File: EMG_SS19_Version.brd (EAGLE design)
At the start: 160 x 100 mm, 219 parts, among them SW1 B3S-1000, SW2 B3S-1000, SW3 B3S-1000, SW4 B3S-1000, SW5 B3S-1000, T11 OPA388, T12 OPA388, T21 OPA388, T22 OPA388

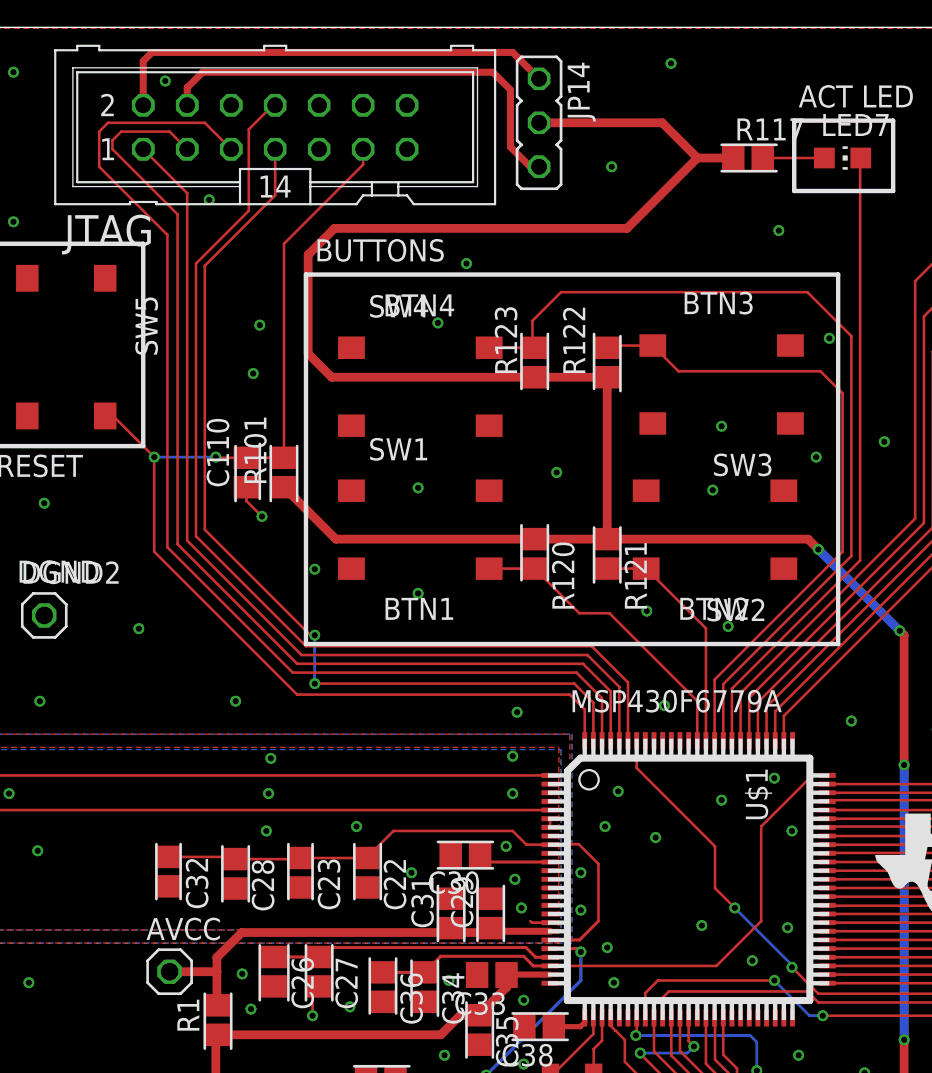
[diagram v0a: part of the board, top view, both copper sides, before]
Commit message: Fixed 3 buttons Added UART as back-channel to JTAG header acc. http://www.ti.com/lit/ug/slau647m/slau647m.pdf p.19
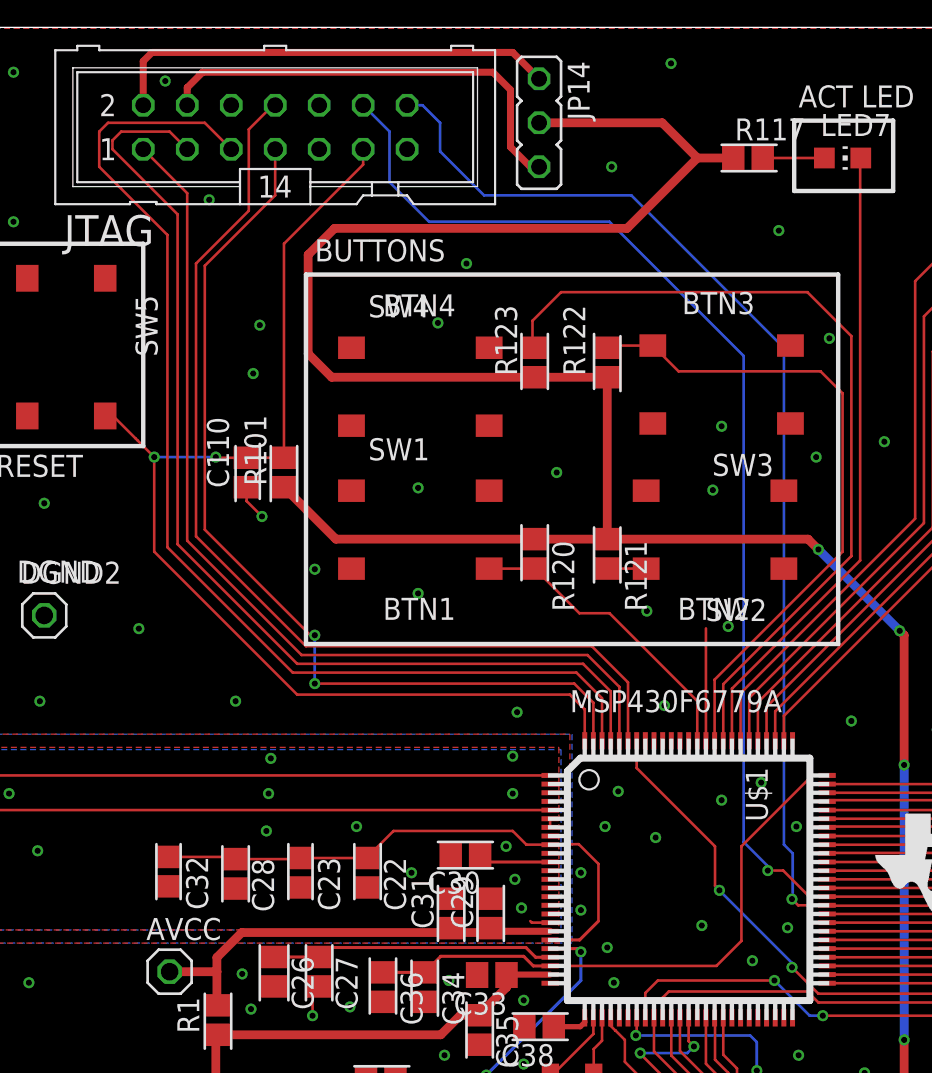
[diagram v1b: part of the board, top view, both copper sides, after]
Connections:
- removed net N$56: SW2.1
- removed net P4.1: P4.2, U$1.60
- removed net P4.2: P4.3, U$1.61
- new net UART_CTS: JTAG.10
- new net UART_RTS: JTAG.13
- new net UART_RX: JTAG.14, P4.2, U$1.60
- new net UART_TX: JTAG.12, P4.3, U$1.61
- net BTN2: now also SW2.1; no longer SW2.3
- net BTN4: now also SW4.1; no longer SW4.3
- net RESET: now also SW5.1; no longer SW5.3
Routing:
- net UART_TX: track 0.00 -> 82.7 mm, vias 0 -> 1
- net UART_RX: track 0.00 -> 82.3 mm, vias 0 -> 1
- net P4.1: track 19.5 -> 0.00 mm
- net P4.2: track 18.6 -> 0.00 mm
- net BTN2: track 13.6 -> 8.74 mm
- net BTN4: track 50.9 -> 48.6 mm
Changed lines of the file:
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@@
 <?xml version="1.0" encoding="utf-8"?>
 <!DOCTYPE eagle SYSTEM "eagle.dtd">
-<eagle version="9.4.2">
+<eagle version="9.4.1">
 <drawing>
 <settings>
@@
 <via x="117.729" y="44.958" extent="1-16" drill="0.35"/>
 <via x="132.334" y="48.133" extent="1-16" drill="0.35"/>
-<via x="137.541" y="53.594" extent="1-16" drill="0.35"/>
+<via x="137.795" y="53.848" extent="1-16" drill="0.35"/>
 <via x="133.477" y="55.372" extent="1-16" drill="0.35"/>
 <via x="145.415" y="33.782" extent="1-16" drill="0.35"/>
@@
 <via x="135.255" y="46.101" extent="1-16" drill="0.35"/>
 <via x="137.287" y="48.006" extent="1-16" drill="0.35"/>
-<via x="136.525" y="56.642" extent="1-16" drill="0.35"/>
+<via x="135.763" y="56.388" extent="1-16" drill="0.35"/>
 <via x="126.873" y="46.863" extent="1-16" drill="0.35"/>
 <via x="125.349" y="49.022" extent="1-16" drill="0.35"/>
@@
 <wire x1="124.714" y1="61.468" x2="108.966" y2="61.468" width="0.1524" layer="1"/>
 <wire x1="108.966" y1="61.468" x2="100.711" y2="69.723" width="0.1524" layer="1"/>
-<contactref element="SW5" pad="3"/>
-<wire x1="97.881" y1="77.559" x2="98.336" y2="77.559" width="0.1524" layer="1"/>
 <wire x1="98.336" y1="77.559" x2="99.649" y2="76.246" width="0.1524" layer="1"/>
+<contactref element="SW5" pad="1"/>
+<wire x1="93.381" y1="77.559" x2="98.336" y2="77.559" width="0" layer="19" extent="1-1"/>
 </signal>
 <signal name="TEST/SBWTCK">
@@
 <contactref element="R121" pad="2"/>
 <contactref element="U$1" pad="86"/>
-<contactref element="SW2" pad="3"/>
 <wire x1="126.873" y1="68.746" x2="129.118" y2="68.746" width="0.1524" layer="1"/>
-<wire x1="129.118" y1="68.746" x2="129.121" y2="68.743" width="0.1524" layer="1"/>
-<wire x1="132.572" y1="65.292" x2="129.121" y2="68.743" width="0.1524" layer="1"/>
 <wire x1="132.572" y1="58.8" x2="132.572" y2="65.292" width="0.1524" layer="1"/>
+<contactref element="SW2" pad="1"/>
+<wire x1="129.118" y1="68.746" x2="129.121" y2="73.243" width="0" layer="19" extent="1-1"/>
+<wire x1="132.572" y1="65.292" x2="129.118" y2="68.746" width="0" layer="19" extent="1-1"/>
 </signal>
 <signal name="BTN4">
@@
 <wire x1="133.572" y1="62.071" x2="140.97" y2="69.469" width="0.1524" layer="1"/>
 <wire x1="140.97" y1="69.469" x2="140.97" y2="82.169" width="0.1524" layer="1"/>
-<contactref element="SW4" pad="3"/>
-<wire x1="120.053" y1="81.498" x2="122.392" y2="81.498" width="0.1524" layer="1"/>
 <wire x1="122.392" y1="81.498" x2="122.555" y2="81.661" width="0.1524" layer="1"/>
+<contactref element="SW4" pad="1"/>
+<wire x1="122.392" y1="81.498" x2="120.053" y2="76.998" width="0" layer="19" extent="1-1"/>
 </signal>
 <signal name="LED1">
@@
 <contactref element="U$1" pad="94"/>
 <wire x1="128.572" y1="58.8" x2="128.572" y2="57.229" width="0.1524" layer="1"/>
-<wire x1="133.096" y1="52.705" x2="133.096" y2="50.292" width="0.1524" layer="1"/>
-<wire x1="133.096" y1="50.292" x2="134.239" y2="49.149" width="0.1524" layer="1"/>
+<wire x1="133.096" y1="52.705" x2="133.096" y2="50.419" width="0.1524" layer="1"/>
+<wire x1="133.096" y1="50.419" x2="133.35" y2="50.165" width="0.1524" layer="1"/>
 <wire x1="128.572" y1="57.229" x2="133.096" y2="52.705" width="0.1524" layer="1"/>
-<via x="134.239" y="49.149" extent="1-16" drill="0.35"/>
-<wire x1="137.541" y1="45.847" x2="134.239" y2="49.149" width="0.1524" layer="16"/>
-<wire x1="137.541" y1="45.847" x2="137.541" y2="45.72" width="0.1524" layer="16"/>
+<via x="133.35" y="50.165" extent="1-16" drill="0.35"/>
+<wire x1="137.541" y1="45.974" x2="133.35" y2="50.165" width="0.1524" layer="16"/>
+<wire x1="137.541" y1="45.974" x2="137.541" y2="45.72" width="0.1524" layer="16"/>
 <via x="137.541" y="45.72" extent="1-16" drill="0.35"/>
 <wire x1="139.065" y1="44.196" x2="146.812" y2="44.196" width="0.1524" layer="1"/>
@@
 <wire x1="116.332" y1="45.427" x2="113.919" y2="45.427" width="0.1778" layer="1"/>
 <wire x1="123.572" y1="45.8" x2="133.176" y2="45.8" width="0.1524" layer="1"/>
-<wire x1="135.763" y1="48.387" x2="135.763" y2="53.848" width="0.1524" layer="1"/>
-<wire x1="135.763" y1="53.848" x2="138.715" y2="56.8" width="0.1524" layer="1"/>
+<wire x1="134.62" y1="47.244" x2="134.62" y2="52.705" width="0.1524" layer="1"/>
+<wire x1="134.62" y1="52.705" x2="138.715" y2="56.8" width="0.1524" layer="1"/>
 <wire x1="138.715" y1="56.8" x2="139.572" y2="56.8" width="0.1524" layer="1"/>
-<wire x1="133.176" y1="45.8" x2="135.763" y2="48.387" width="0.1524" layer="1"/>
+<wire x1="133.176" y1="45.8" x2="134.62" y2="47.244" width="0.1524" layer="1"/>
 </signal>
 <signal name="AVCC">
@@
 <wire x1="144.653" y1="71.628" x2="144.653" y2="85.344" width="0.1524" layer="1"/>
 </signal>
-<signal name="P4.1">
-<contactref element="U$1" pad="60"/>
-<contactref element="P4" pad="2"/>
-<wire x1="139.572" y1="49.3" x2="139.596" y2="49.276" width="0.1524" layer="1"/>
-<wire x1="139.596" y1="49.276" x2="149.352" y2="49.276" width="0.1524" layer="1"/>
-<wire x1="149.352" y1="49.276" x2="156.21" y2="42.418" width="0.1524" layer="1"/>
-</signal>
-<signal name="P4.2">
-<contactref element="U$1" pad="61"/>
-<contactref element="P4" pad="3"/>
-<wire x1="154.432" y1="44.958" x2="156.21" y2="44.958" width="0.1524" layer="1"/>
-<wire x1="139.572" y1="49.8" x2="149.59" y2="49.8" width="0.1524" layer="1"/>
-<wire x1="149.59" y1="49.8" x2="154.432" y2="44.958" width="0.1524" layer="1"/>
-</signal>
 <signal name="P4.3">
 <contactref element="U$1" pad="62"/>
@@
 <wire x1="62.23" y1="80.96" x2="62.23" y2="81.6" width="0.1524" layer="1"/>
 </signal>
-<signal name="N$56">
-<contactref element="SW2" pad="1"/>
+<signal name="UART_CTS">
+<contactref element="JTAG" pad="10"/>
+</signal>
+<signal name="UART_TX">
+<contactref element="JTAG" pad="12"/>
+<contactref element="U$1" pad="61"/>
+<contactref element="P4" pad="3"/>
+<wire x1="154.432" y1="44.958" x2="156.21" y2="44.958" width="0.1524" layer="1"/>
+<wire x1="139.572" y1="49.8" x2="149.59" y2="49.8" width="0.1524" layer="1"/>
+<wire x1="149.59" y1="49.8" x2="154.432" y2="44.958" width="0.1524" layer="1"/>
+<wire x1="139.572" y1="49.8" x2="138.541" y2="49.8" width="0.1524" layer="1"/>
+<wire x1="137.033" y1="51.308" x2="136.144" y2="51.308" width="0.1524" layer="1"/>
+<via x="136.144" y="51.308" extent="1-16" drill="0.35"/>
+<wire x1="136.144" y1="51.308" x2="136.144" y2="51.562" width="0.1524" layer="16"/>
+<wire x1="136.144" y1="51.562" x2="134.747" y2="52.959" width="0.1524" layer="16"/>
+<wire x1="134.747" y1="52.959" x2="134.747" y2="81.026" width="0.1524" layer="16"/>
+<wire x1="134.747" y1="81.026" x2="127" y2="88.773" width="0.1524" layer="16"/>
+<wire x1="127" y1="88.773" x2="116.586" y2="88.773" width="0.1524" layer="16"/>
+<wire x1="116.586" y1="88.773" x2="114.3" y2="91.059" width="0.1524" layer="16"/>
+<wire x1="114.3" y1="93.98" x2="112.776" y2="95.504" width="0.1524" layer="16"/>
+<wire x1="138.541" y1="49.8" x2="137.033" y2="51.308" width="0.1524" layer="1"/>
+<wire x1="114.3" y1="91.059" x2="114.3" y2="93.98" width="0.1524" layer="16"/>
+</signal>
+<signal name="UART_RX">
+<contactref element="JTAG" pad="14"/>
+<contactref element="U$1" pad="60"/>
+<contactref element="P4" pad="2"/>
+<wire x1="139.572" y1="49.3" x2="139.596" y2="49.276" width="0.1524" layer="1"/>
+<wire x1="139.596" y1="49.276" x2="149.352" y2="49.276" width="0.1524" layer="1"/>
+<wire x1="149.352" y1="49.276" x2="156.21" y2="42.418" width="0.1524" layer="1"/>
+<wire x1="139.572" y1="49.3" x2="137.898" y2="49.3" width="0.1524" layer="1"/>
+<wire x1="137.898" y1="49.3" x2="137.541" y2="49.657" width="0.1524" layer="1"/>
+<via x="137.541" y="49.657" extent="1-16" drill="0.35"/>
+<wire x1="137.5842" y1="52.29831875" x2="137.5842" y2="49.7002" width="0.1524" layer="16"/>
+<wire x1="137.541" y1="49.657" x2="137.5842" y2="49.7002" width="0.1524" layer="16"/>
+<wire x1="137.0762" y1="52.80631875" x2="137.0762" y2="81.4908" width="0.1524" layer="16"/>
+<wire x1="137.5842" y1="52.29831875" x2="137.0762" y2="52.80631875" width="0.1524" layer="16"/>
+<wire x1="128.27" y1="90.297" x2="119.761" y2="90.297" width="0.1524" layer="16"/>
+<wire x1="119.761" y1="90.297" x2="117.221" y2="92.837" width="0.1524" layer="16"/>
+<wire x1="117.221" y1="92.837" x2="117.221" y2="94.488" width="0.1524" layer="16"/>
+<wire x1="117.221" y1="94.488" x2="116.205" y2="95.504" width="0.1524" layer="16"/>
+<wire x1="116.205" y1="95.504" x2="115.316" y2="95.504" width="0.1524" layer="16"/>
+<wire x1="137.0762" y1="81.4908" x2="128.27" y2="90.297" width="0.1524" layer="16"/>
+</signal>
+<signal name="UART_RTS">
+<contactref element="JTAG" pad="13"/>
 </signal>
 </signals>
